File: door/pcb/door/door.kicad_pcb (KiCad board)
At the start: 2 copper layers, 73.2 x 35.1 mm, 42 parts, among them J1 USB_B_Micro, J2 Conn_01x06_Male, J3 DB9_Female_MountingHoles, J4 Conn_01x03_Male, J5 Screw_Terminal_01x02, J6 Screw_Terminal_01x02, U1 LM1117-3.3, U2 STM32F303CBTx, U3 SN65HVD230, Y1 8 Mhz

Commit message: usb stecker getauscht
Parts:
- J1: footprint Connector_USB:USB_Micro-B_Amphenol_10103594-0001LF_Horizontal -> Connector_USB:USB_Micro-B_Wuerth_629105150521
- moved J1 0.27 mm to (152.9, 101.4)
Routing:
- net GND: track 55.1 -> 51.1 mm, vias 28 -> 31

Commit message: caps voltage regulator gestauscht
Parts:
- C1: footprint Capacitor_SMD:C_0805_2012Metric -> Capacitor_Tantalum_SMD:CP_EIA-3216-10_Kemet-I
- C2: value 100uF -> 10uF; footprint Capacitor_SMD:C_0805_2012Metric -> Capacitor_Tantalum_SMD:CP_EIA-3216-10_Kemet-I
- U1: value LM1117-3.3 -> 10uF

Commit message: Taster
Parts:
- turned R2 to 90 degrees
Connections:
- R2 pad 1: +3V3 -> /mcu/SW2
- R2 pad 2: /mcu/SW2 -> +3V3
- S1 pad 1: GND -> Net-(S1-Pad1)
- S1 pad 3: NRST -> Net-(S1-Pad3)
- S2 pad 1: GND -> Net-(S2-Pad1)
- S2 pad 3: /mcu/SW2 -> Net-(S2-Pad3)
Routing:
- net GND: track 51.1 -> 46.0 mm
- net NRST: track 62.9 -> 58.8 mm
- net /mcu/SW2: track 34.6 -> 30.5 mm
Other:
- net class +3V3: clearance 0.152 -> 0.1524
- net class +5V: clearance 0.152 -> 0.1524
- net class Default: clearance 0.152 -> 0.1524
- net class GND: clearance 0.152 -> 0.1524
- net class motor_out: clearance 0.152 -> 0.1524
- rule trace_clearance: 0.152 -> 0.1524
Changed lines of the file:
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@@
     (thickness 1.6)
     (drawings 24)
-    (tracks 344)
+    (tracks 336)
     (zones 0)
     (modules 42)
-    (nets 70)
+    (nets 74)
   )
   (page A4)
@@
   (setup
     (last_trace_width 0.25)
-    (trace_clearance 0.152)
+    (trace_clearance 0.1524)
     (zone_clearance 0.1524)
     (zone_45_only no)
@@
     (pcbplotparams
       (layerselection 0x010fc_ffffffff)
-      (usegerberextensions false)
+      (usegerberextensions true)
       (usegerberattributes false)
       (usegerberadvancedattributes false)
@@
   (net 68 /mcu/CANL)
   (net 69 /mcu/SW2)
+  (net 70 "Net-(S1-Pad1)")
+  (net 71 "Net-(S1-Pad3)")
+  (net 72 "Net-(S2-Pad3)")
+  (net 73 "Net-(S2-Pad1)")
   (net_class Default "This is the default net class."
-    (clearance 0.152)
+    (clearance 0.1524)
     (trace_width 0.25)
     (via_dia 0.8)
@@
     (add_net "Net-(JP1-Pad2)")
     (add_net "Net-(R8-Pad1)")
+    (add_net "Net-(S1-Pad1)")
+    (add_net "Net-(S1-Pad3)")
+    (add_net "Net-(S2-Pad1)")
+    (add_net "Net-(S2-Pad3)")
     (add_net "Net-(U2-Pad1)")
     (add_net "Net-(U2-Pad10)")
@@
   )
   (net_class +3V3 ""
-    (clearance 0.152)
+    (clearance 0.1524)
     (trace_width 0.25)
     (via_dia 0.8)
@@
   )
   (net_class +5V ""
-    (clearance 0.152)
+    (clearance 0.1524)
     (trace_width 0.25)
     (via_dia 0.8)
@@
   )
   (net_class GND ""
-    (clearance 0.152)
+    (clearance 0.1524)
     (trace_width 0.25)
     (via_dia 0.8)
@@
   )
   (net_class motor_out ""
-    (clearance 0.152)
+    (clearance 0.1524)
     (trace_width 0.625)
     (via_dia 0.8)
@@
     (descr "Pololu Breakout 16-pin 15.2x20.3mm 0.6x0.8\\")
     (tags "Pololu Breakout")
-    (fp_text reference A1 (at 8.382 20.066 270) (layer F.SilkS)
+    (fp_text reference A1 (at 9.398 20.066 270) (layer F.SilkS)
       (effects (font (size 1 1) (thickness 0.15)))
     )
@@
   )
   (module Resistor_SMD:R_0805_2012Metric (layer F.Cu)
-    (at 180.5686 108.4857 270)
+    (at 180.5686 108.4857 90)
     (descr "Resistor SMD 0805 (2012 Metric), square (rectangular) end terminal, IPC_7351 nominal, (Body size source: https://docs.google.com/spreadsheets/d/1BsfQQcO9C6DZCsRaXUlFlo91Tg2WpOkGARC1WS5S8t0/edit?usp=sharing), generated with kicad-footprint-generator")
     (tags resistor)
     (attr smd)
-    (fp_text reference R2 (at 3.4775 0.0508 270) (layer F.SilkS)
-      (effects (font (size 1 1) (thickness 0.15)))
-    )
-    (fp_text value 4k7 (at 0 1.65 270) (layer F.Fab)
-      (effects (font (size 1 1) (thickness 0.15)))
-    )
-    (fp_text user %R (at 0 0 270) (layer F.Fab)
+    (fp_text reference R2 (at -3.2743 0.0508 90) (layer F.SilkS)
+      (effects (font (size 1 1) (thickness 0.15)))
+    )
+    (fp_text value 4k7 (at 0 1.65 90) (layer F.Fab)
+      (effects (font (size 1 1) (thickness 0.15)))
+    )
+    (fp_text user %R (at 0 0 90) (layer F.Fab)
       (effects (font (size 0.5 0.5) (thickness 0.08)))
     )
@@
     (fp_line (start -1 -0.6) (end 1 -0.6) (layer F.Fab) (width 0.1))
     (fp_line (start -1 0.6) (end -1 -0.6) (layer F.Fab) (width 0.1))
-    (pad 2 smd roundrect (at 0.9375 0 270) (size 0.975 1.4) (layers F.Cu F.Paste F.Mask) (roundrect_rratio 0.25)
+    (pad 2 smd roundrect (at 0.9375 0 90) (size 0.975 1.4) (layers F.Cu F.Paste F.Mask) (roundrect_rratio 0.25)
+      (net 3 +3V3))
+    (pad 1 smd roundrect (at -0.9375 0 90) (size 0.975 1.4) (layers F.Cu F.Paste F.Mask) (roundrect_rratio 0.25)
       (net 69 /mcu/SW2))
-    (pad 1 smd roundrect (at -0.9375 0 270) (size 0.975 1.4) (layers F.Cu F.Paste F.Mask) (roundrect_rratio 0.25)
-      (net 3 +3V3))
     (model ${KISYS3DMOD}/Resistor_SMD.3dshapes/R_0805_2012Metric.wrl
       (at (xyz 0 0 0))
@@
     (fp_circle (center 0 0) (end 0 -0.80264) (layer F.SilkS) (width 0.127))
     (pad 1 smd rect (at -2.04978 0.79756 180) (size 0.89916 0.99822) (layers F.Cu F.Paste F.Mask)
-      (net 1 GND) (solder_mask_margin 0.1016))
+      (net 70 "Net-(S1-Pad1)") (solder_mask_margin 0.1016))
     (pad 2 smd rect (at 2.04978 0.79756 180) (size 0.89916 0.99822) (layers F.Cu F.Paste F.Mask)
       (net 1 GND) (solder_mask_margin 0.1016))
     (pad 3 smd rect (at 2.04978 -0.79756 180) (size 0.89916 0.99822) (layers F.Cu F.Paste F.Mask)
-      (net 59 NRST) (solder_mask_margin 0.1016))
+      (net 71 "Net-(S1-Pad3)") (solder_mask_margin 0.1016))
     (pad 4 smd rect (at -2.04978 -0.79756 180) (size 0.89916 0.99822) (layers F.Cu F.Paste F.Mask)
       (net 59 NRST) (solder_mask_margin 0.1016))
@@
       (net 69 /mcu/SW2) (solder_mask_margin 0.1016))
     (pad 3 smd rect (at 2.04978 -0.79756 180) (size 0.89916 0.99822) (layers F.Cu F.Paste F.Mask)
-      (net 69 /mcu/SW2) (solder_mask_margin 0.1016))
+      (net 72 "Net-(S2-Pad3)") (solder_mask_margin 0.1016))
     (pad 2 smd rect (at 2.04978 0.79756 180) (size 0.89916 0.99822) (layers F.Cu F.Paste F.Mask)
       (net 1 GND) (solder_mask_margin 0.1016))
     (pad 1 smd rect (at -2.04978 0.79756 180) (size 0.89916 0.99822) (layers F.Cu F.Paste F.Mask)
-      (net 1 GND) (solder_mask_margin 0.1016))
+      (net 73 "Net-(S2-Pad1)") (solder_mask_margin 0.1016))
   )
   (module TestPoint:TestPoint_Loop_D1.80mm_Drill1.0mm_Beaded (layer F.Cu)
@@
   (via (at 159.4612 120.5484) (size 0.8) (drill 0.3) (layers F.Cu B.Cu) (net 1))
   (segment (start 159.01016 120.5484) (end 159.4612 120.5484) (width 0.25) (layer F.Cu) (net 1))
-  (segment (start 160.25876 119.75084) (end 159.4612 120.5484) (width 0.25) (layer F.Cu) (net 1))
-  (segment (start 161.61258 119.75084) (end 160.25876 119.75084) (width 0.25) (layer F.Cu) (net 1))
   (via (at 169.7228 120.65) (size 0.8) (drill 0.3) (layers F.Cu B.Cu) (net 1))
   (segment (start 167.80764 119.75084) (end 168.82364 119.75084) (width 0.25) (layer F.Cu) (net 1))
   (segment (start 168.82364 119.75084) (end 169.7228 120.65) (width 0.25) (layer F.Cu) (net 1))
-  (segment (start 170.62196 119.75084) (end 169.7228 120.65) (width 0.25) (layer F.Cu) (net 1))
-  (segment (start 171.9072 119.75084) (end 170.62196 119.75084) (width 0.25) (layer F.Cu) (net 1))
   (via (at 166.2176 119.8372) (size 0.8) (drill 0.3) (layers F.Cu B.Cu) (net 1))
   (segment (start 164.7952 119.791) (end 166.1714 119.791) (width 0.25) (layer F.Cu) (net 1))
@@
   (segment (start 166.176201 123.047001) (end 200.218799 123.047001) (width 0.25) (layer F.Cu) (net 59))
   (segment (start 164.7952 121.666) (end 166.176201 123.047001) (width 0.25) (layer F.Cu) (net 59))
-  (segment (start 158.2126 121.34596) (end 161.61258 121.34596) (width 0.25) (layer F.Cu) (net 59))
-  (segment (start 157.51302 121.34596) (end 158.2126 121.34596) (width 0.25) (layer F.Cu) (net 59))
   (segment (start 203.277174 109.47716) (end 203.677173 109.077161) (width 0.25) (layer F.Cu) (net 59))
   (via (at 203.677173 109.077161) (size 0.8) (drill 0.3) (layers F.Cu B.Cu) (net 59))
@@
   (segment (start 180.5686 109.4232) (end 181.99811 107.99369) (width 0.25) (layer F.Cu) (net 69))
   (segment (start 181.99811 107.99369) (end 190.41719 107.99369) (width 0.25) (layer F.Cu) (net 69))
-  (segment (start 168.50722 121.34596) (end 171.9072 121.34596) (width 0.25) (layer F.Cu) (net 69))
-  (segment (start 167.80764 121.34596) (end 168.50722 121.34596) (width 0.25) (layer F.Cu) (net 69))
   (zone (net 1) (net_name GND) (layer B.Cu) (hatch edge 0.508)
     (connect_pads (clearance 0.508))

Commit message: beschriftung
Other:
- board text added: "PWR"
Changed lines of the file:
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@@
   (general
     (thickness 1.6)
-    (drawings 24)
+    (drawings 25)
     (tracks 336)
     (zones 0)
@@
     (tags diode)
     (attr smd)
-    (fp_text reference D1 (at 0 -1.82 270) (layer F.SilkS)
+    (fp_text reference D1 (at -0.124 -2.159 270) (layer F.SilkS)
       (effects (font (size 1 1) (thickness 0.15)))
     )
@@
     )
   )
+  (gr_text PWR (at 156.591 92.964 90) (layer F.SilkS)
+    (effects (font (size 0.8 0.8) (thickness 0.1)))
+  )
   (gr_text NRST (at 201.6125 119.761) (layer F.SilkS)

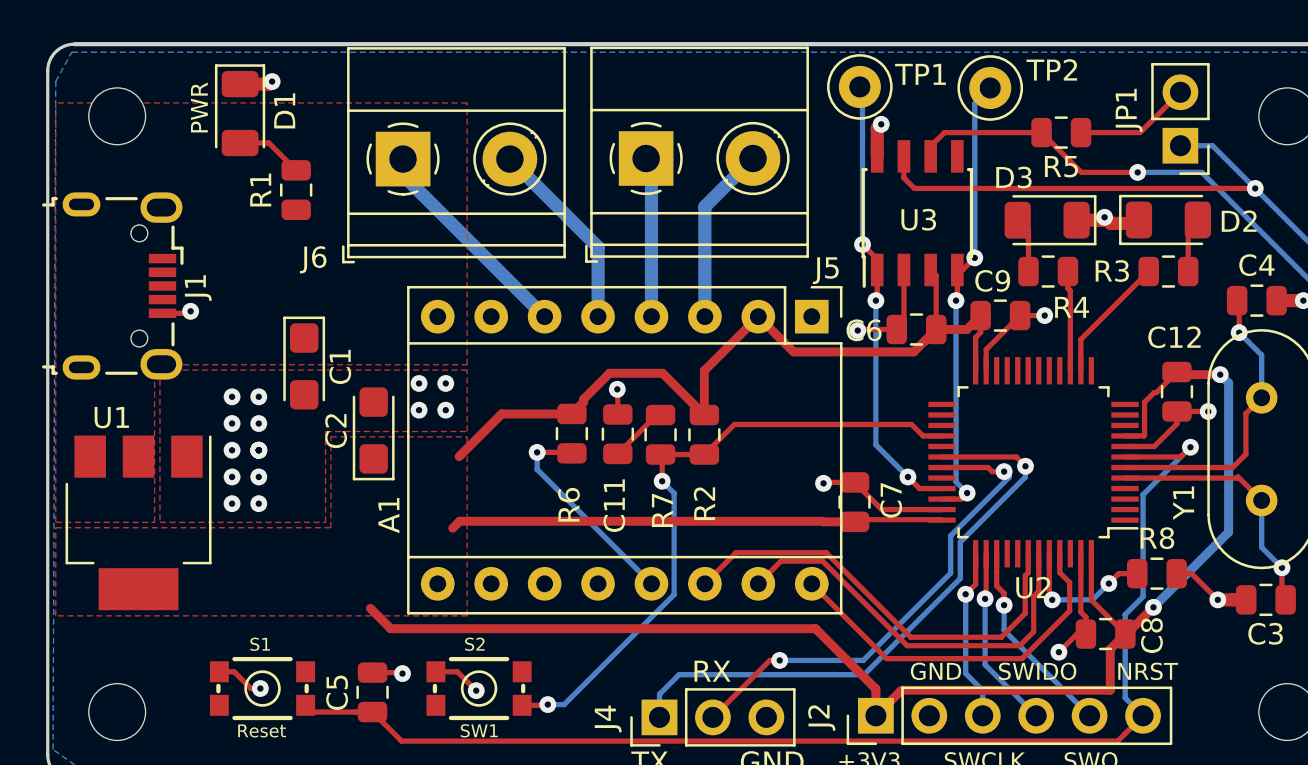
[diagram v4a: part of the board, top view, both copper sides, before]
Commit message: 100uF für Motortreiber geaddet
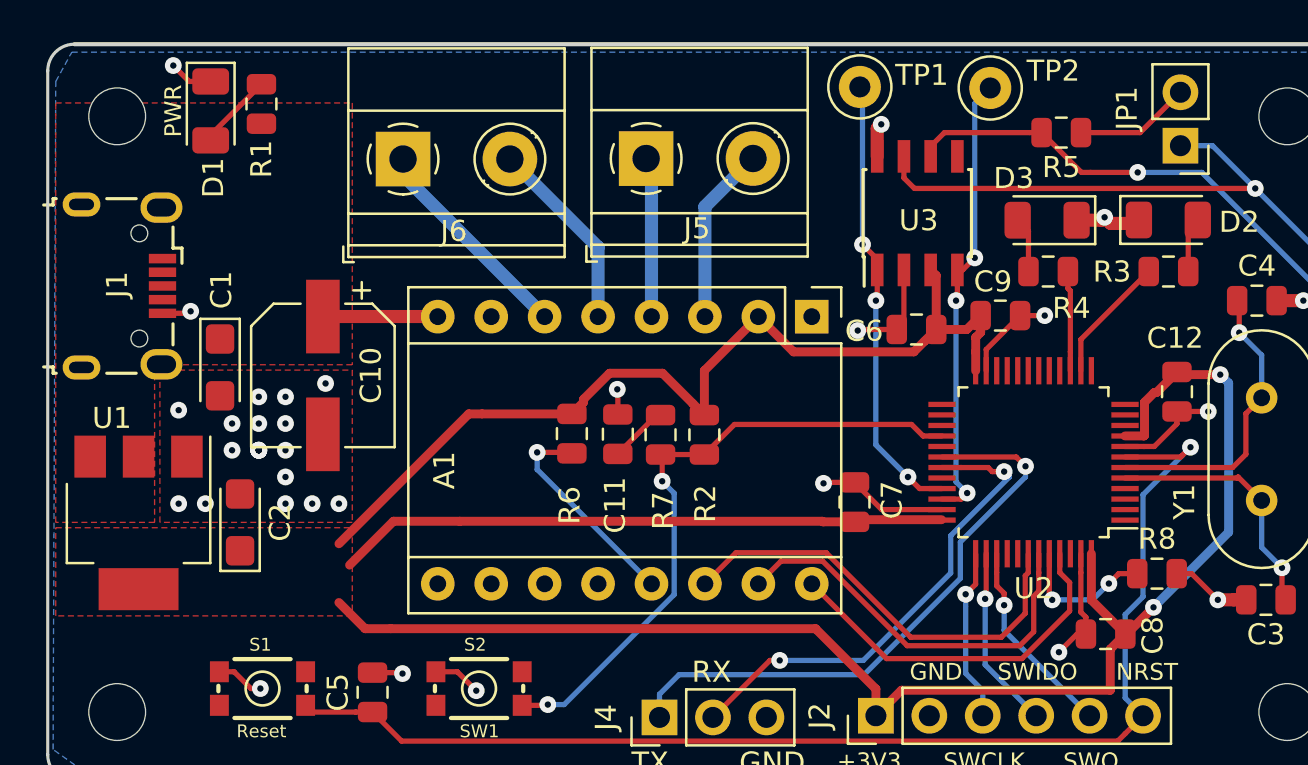
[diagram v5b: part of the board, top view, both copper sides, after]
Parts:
- added C10: 100uF, Capacitor_SMD:CP_Elec_6.3x5.4, F.Cu at (162.4, 105.7)
- moved C2 7.71 mm to (158.5, 112.6)
- moved R1 4.41 mm to (159.5, 92.8)
- moved C1 4.00 mm to (157.5, 105.3)
- moved D1 1.40 mm to (157.1, 93.1)
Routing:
- net +3V3: track 128.5 -> 143.1 mm
- net +5V: track 0.00 -> 5.46 mm
- net GND: track 46.0 -> 46.6 mm, vias 31 -> 33

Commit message: layout überarbeitet
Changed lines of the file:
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@@
     (tags "CMS SOT")
     (attr smd)
-    (fp_text reference U1 (at -4.978 1.27) (layer F.SilkS)
+    (fp_text reference U1 (at -0.279 0) (layer F.SilkS)
       (effects (font (size 1 1) (thickness 0.15)))
     )
@@
     (descr "9-pin D-Sub connector, horizontal/angled (90 deg), THT-mount, female, pitch 2.77x2.84mm, pin-PCB-offset 4.9399999999999995mm, distance of mounting holes 25mm, distance of mounting holes to PCB edge 7.4799999999999995mm, see https://disti-assets.s3.amazonaws.com/tonar/files/datasheets/16730.pdf")
     (tags "9-pin D-Sub connector horizontal angled 90deg THT female pitch 2.77x2.84mm pin-PCB-offset 4.9399999999999995mm mounting-holes-distance 25mm mounting-hole-offset 25mm")
-    (fp_text reference J3 (at -5.54 -3.7 90) (layer F.SilkS)
+    (fp_text reference J3 (at -5.715 5.715 90) (layer F.SilkS)
       (effects (font (size 1 1) (thickness 0.15)))
     )
@@
     (tags "QFP 0.5")
     (attr smd)
-    (fp_text reference U2 (at 0 -6 180) (layer F.SilkS)
+    (fp_text reference U2 (at 0 -0.0635 180) (layer F.SilkS)
       (effects (font (size 1 1) (thickness 0.15)))
     )
@@
     (descr "Crystal THT HC-49/U http://5hertz.com/pdfs/04404_D.pdf")
     (tags "THT crystalHC-49/U")
-    (fp_text reference Y1 (at -0.0635 -3.6703 90) (layer F.SilkS)
-      (effects (font (size 1 1) (thickness 0.15)))
-    )
+    (fp_text reference Y1 (at 2.3876 -0.0508 90) (layer F.SilkS)
+      (effects (font (size 1 1) (thickness 0.15)))
+    )
